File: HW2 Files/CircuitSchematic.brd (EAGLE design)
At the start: 50 x 50 mm, 23 parts

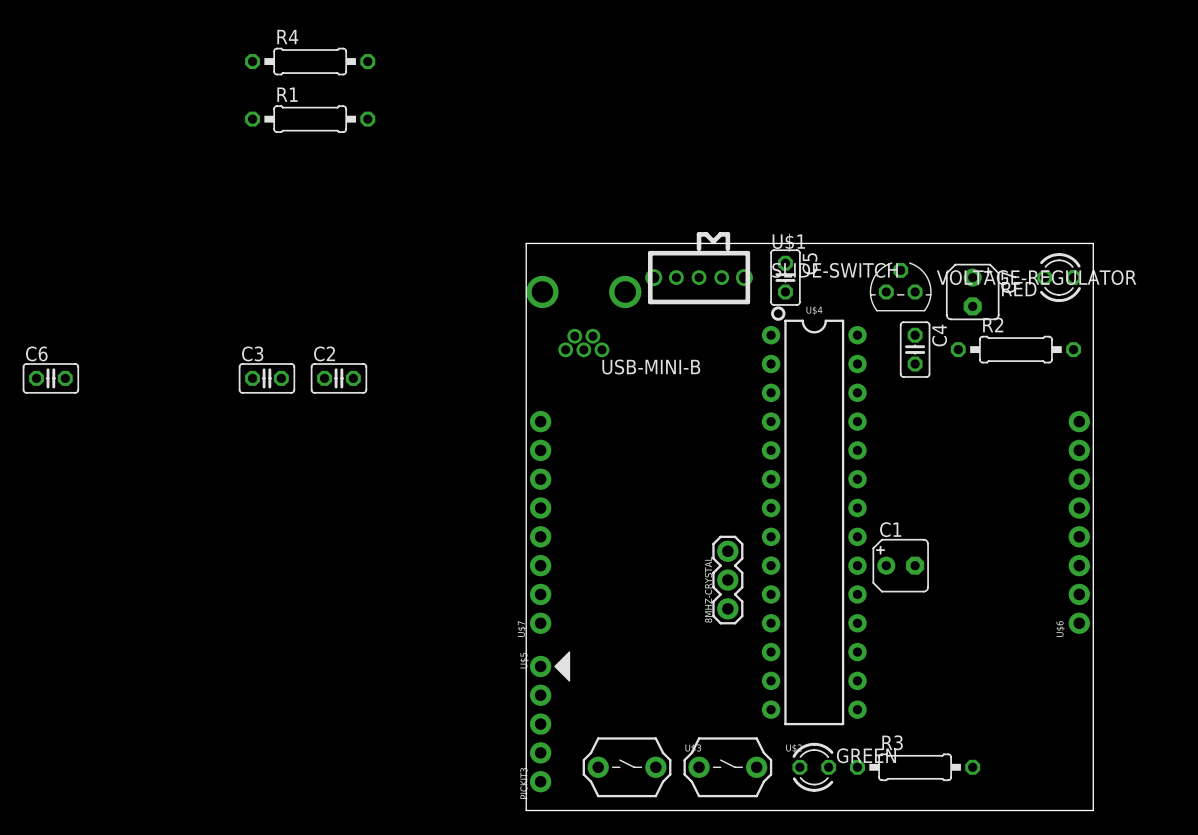
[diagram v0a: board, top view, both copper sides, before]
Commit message: Completed PCB
To Do:
- Add silkscreen pin names
- Error checking
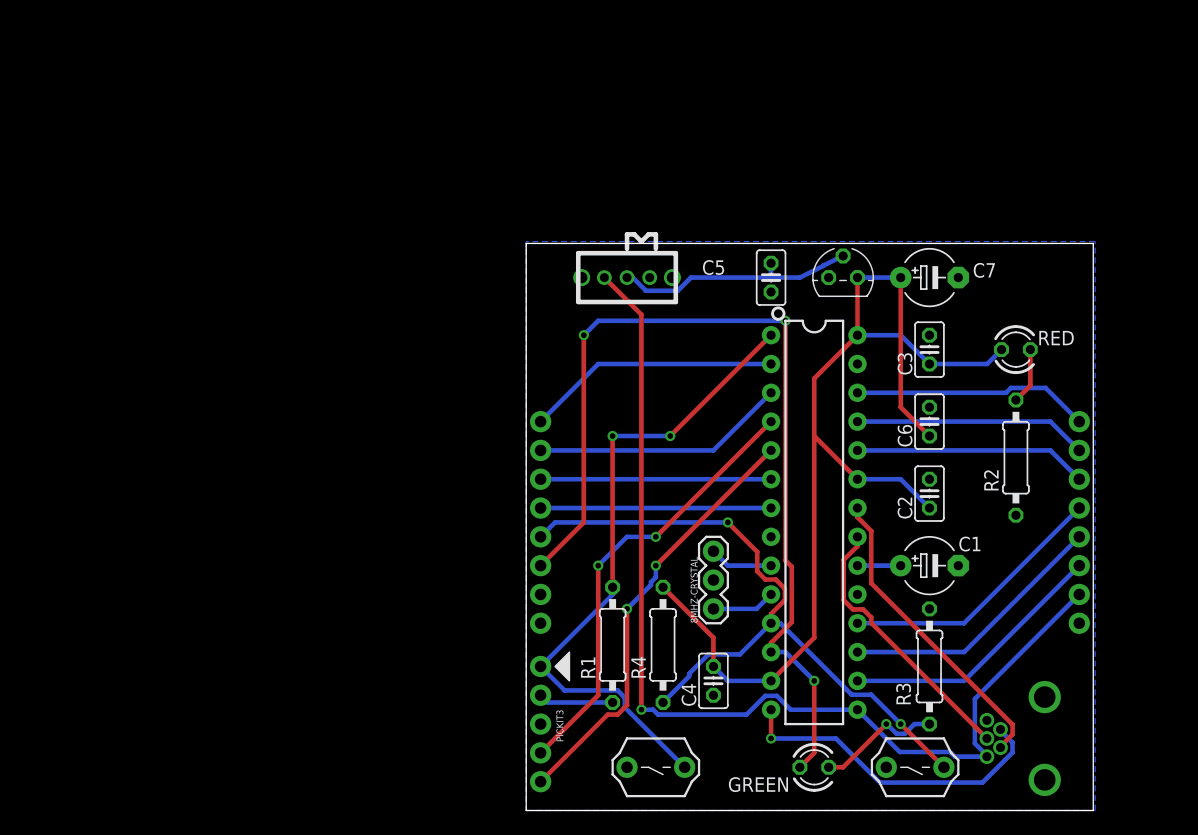
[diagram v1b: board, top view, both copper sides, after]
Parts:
- C1, C7: device resistor:B45181A -> resistor:E5-5
- moved C6 77.6 mm to (35.6, 34.3), turned to 90 degrees
- moved R4 60.1 mm to (12.1, 14.6), turned to 270 degrees
- moved C3 58.5 mm to (35.6, 40.6), turned to 90 degrees
- moved USB-MINI-B 56.6 mm to (45.7, 6.35), turned to 180 degrees
- moved R1 53.5 mm to (7.62, 14.6), turned to 90 degrees
- moved C2 53.1 mm to (35.6, 27.9), turned to 90 degrees
- moved C4 34.2 mm to (16.5, 11.4)
- moved U$3 30.5 mm to (36.8, 3.81), turned to 180 degrees
- moved R2 9.53 mm to (43.2, 31.1), turned to 90 degrees
- moved R3 8.98 mm to (35.6, 12.7), turned to 270 degrees
- moved RED 7.41 mm to (43.2, 40.6), turned to 0 degrees
- moved U$1 6.35 mm to (8.89, 47.0)
- moved VOLTAGE-REGULATOR 5.24 mm to (27.9, 47.0)
- moved C7 4.02 mm to (35.6, 47.0), turned to 0 degrees
- moved C1 2.54 mm to (35.6, 21.6)
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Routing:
- net +3V3: track 0.00 -> 105.7 mm
- net +5V: track 0.00 -> 91.6 mm, vias 0 -> 1
- net A4/LED: track 0.00 -> 83.4 mm, vias 0 -> 3
- net B4/USER: track 0.00 -> 62.1 mm, vias 0 -> 2
- net MCLR: track 0.00 -> 57.5 mm, vias 0 -> 2
- net PGED1: track 0.00 -> 39.1 mm, vias 0 -> 2
- net PGEC1: track 0.00 -> 38.1 mm, vias 0 -> 2
- net USBID: track 0.00 -> 29.0 mm, vias 0 -> 1
- net D-: track 0.00 -> 27.2 mm
- net D+: track 0.00 -> 24.0 mm
- net B9: track 0.00 -> 23.8 mm
- net B8: track 0.00 -> 23.8 mm
- net B7: track 0.00 -> 23.8 mm
- net A1: track 0.00 -> 22.4 mm
- net A0: track 0.00 -> 22.4 mm
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- added copper zone on layer 16, net GND
